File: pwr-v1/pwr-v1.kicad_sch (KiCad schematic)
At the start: 32 parts, among them SW101 SW_SPST, U101 TYPE-C-31-M-12, U102 SK-3296S-01-L1, U103 CH224K, U104 AMS1117-5.0, U105 LM2595S-12, U106 LM2595S-12

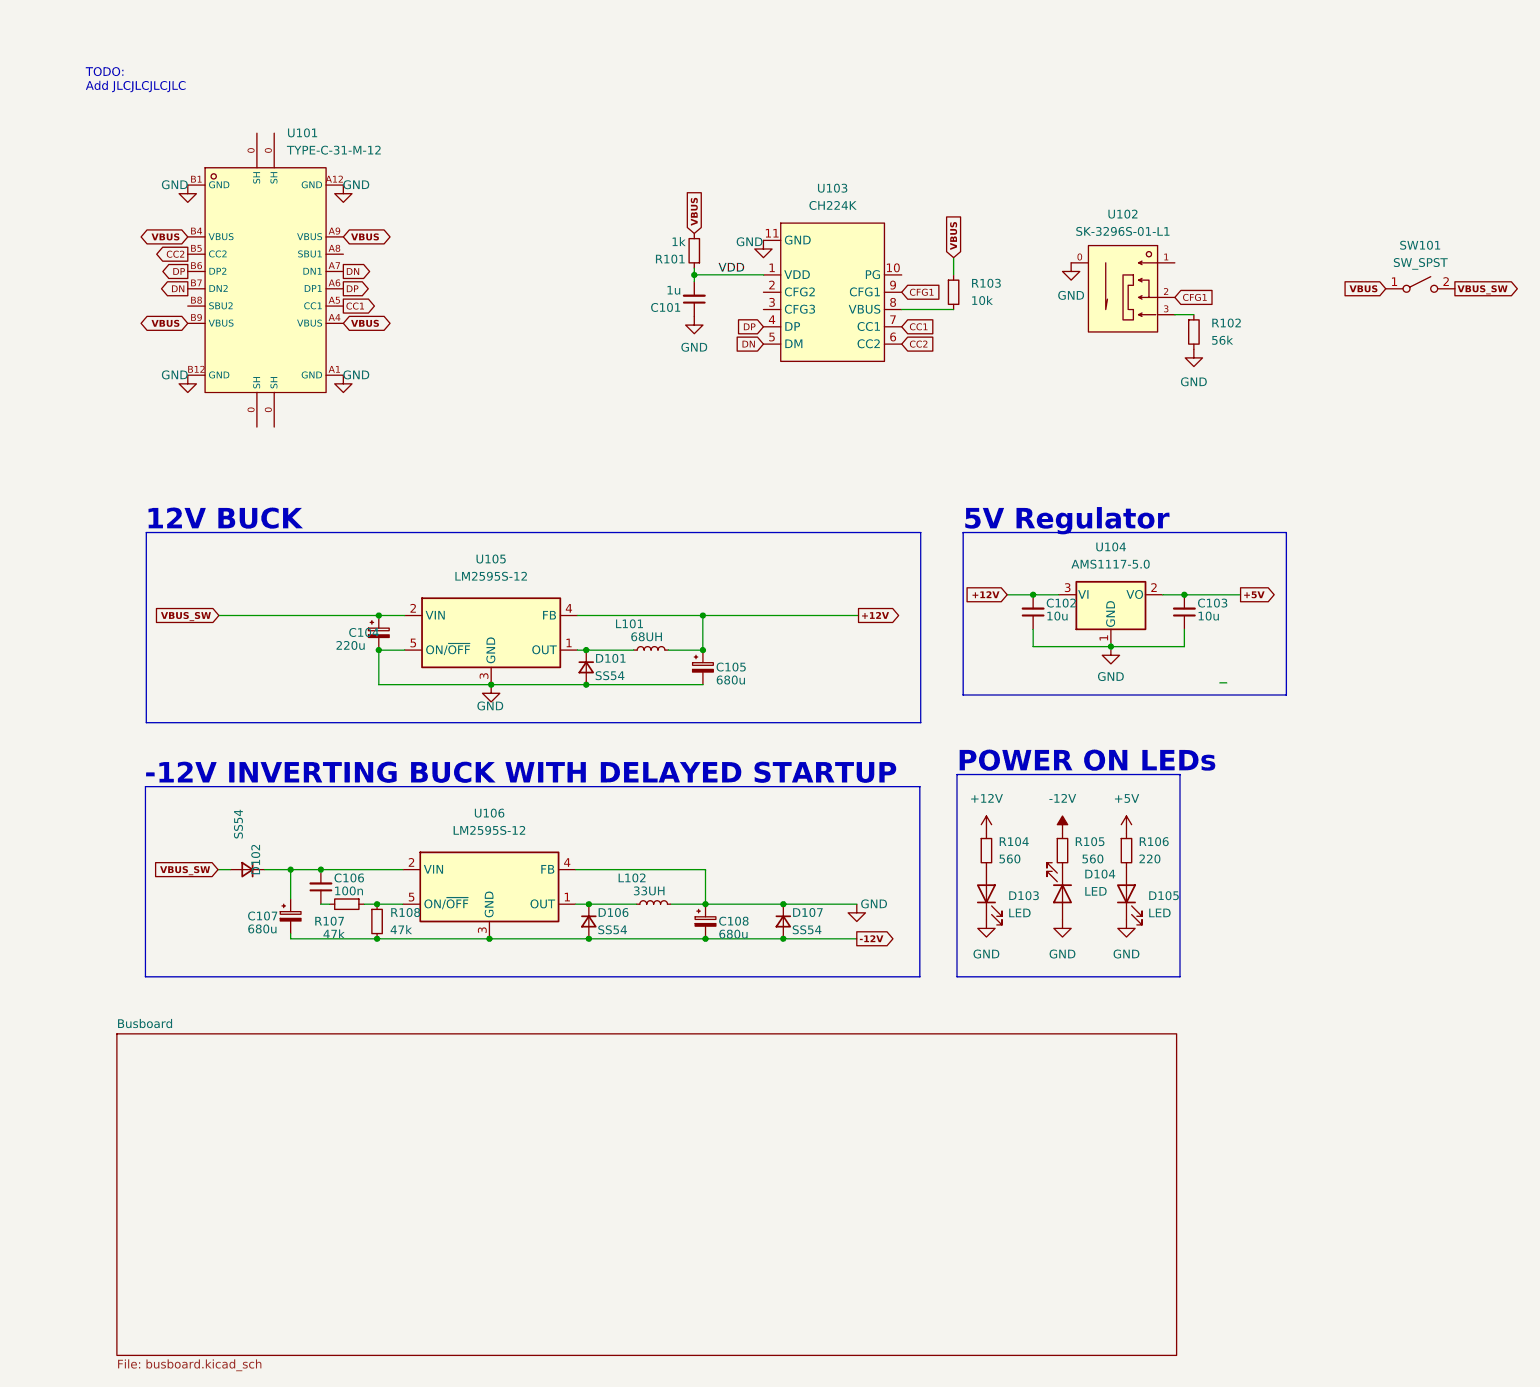
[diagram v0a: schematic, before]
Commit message: Fix bad edgecuts
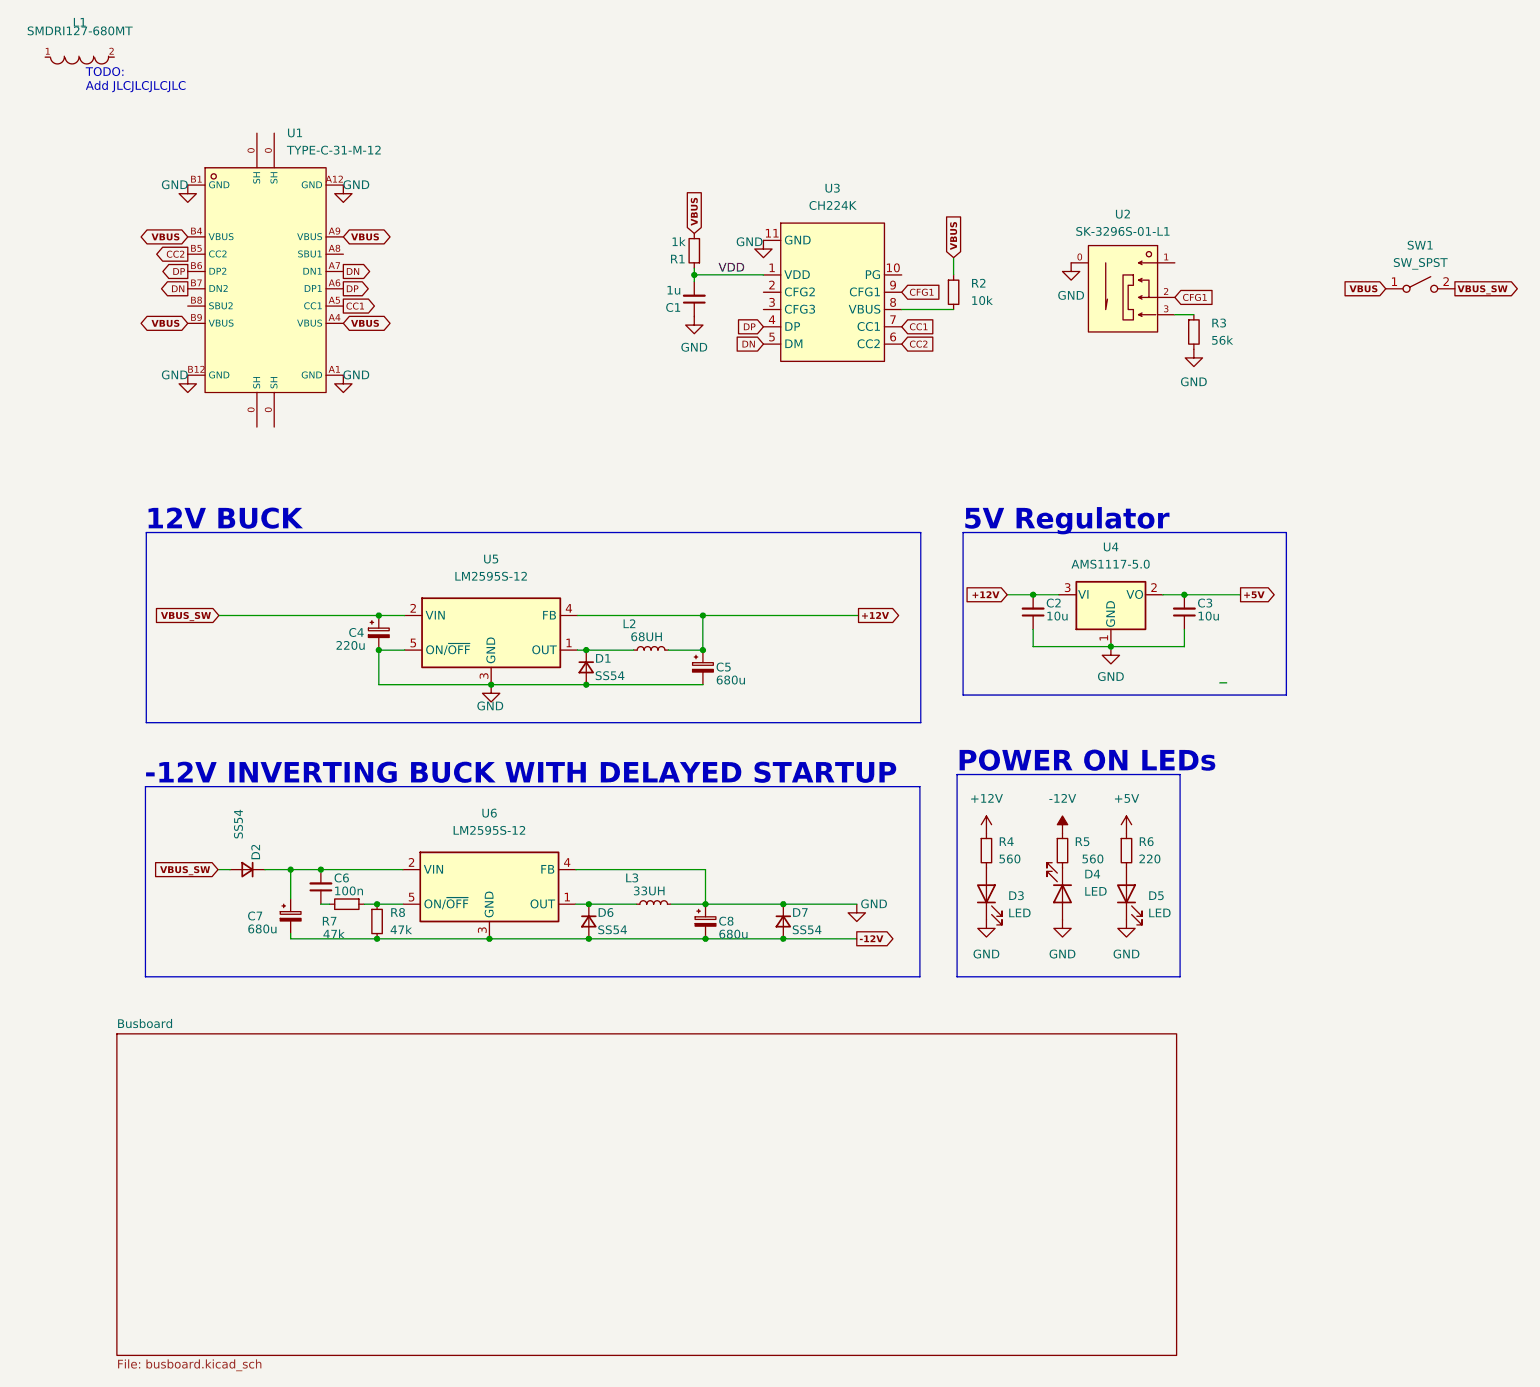
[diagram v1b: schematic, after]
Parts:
- added L1: SMDRI127-680MT, footprint:IND-SMD_L12.3-W12.3_SMDRI127, symbol PWR1LCSC1:SMDRI127-680MT
- renumbered C101 to C1, C102 to C2, C103 to C3, C104 to C4, C105 to C5, C106 to C6, C107 to C7, C108 to C8, D101 to D1, D102 to D2, D103 to D3, D104 to D4, D105 to D5, D106 to D6, D107 to D7, L101 to L2, L102 to L3, R101 to R1, R103 to R2, R102 to R3, R104 to R4, R105 to R5, R106 to R6, R107 to R7, R108 to R8, SW101 to SW1, U101 to U1, U102 to U2, U103 to U3, U104 to U4, U105 to U5, U106 to U6
